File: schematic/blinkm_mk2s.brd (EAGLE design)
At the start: 15.2 x 12.7 mm, 9 parts, among them CN1 1X4SMT, Q1 MOSFET-PCHANNELIRLML2244, U1 ATTINY44QFN

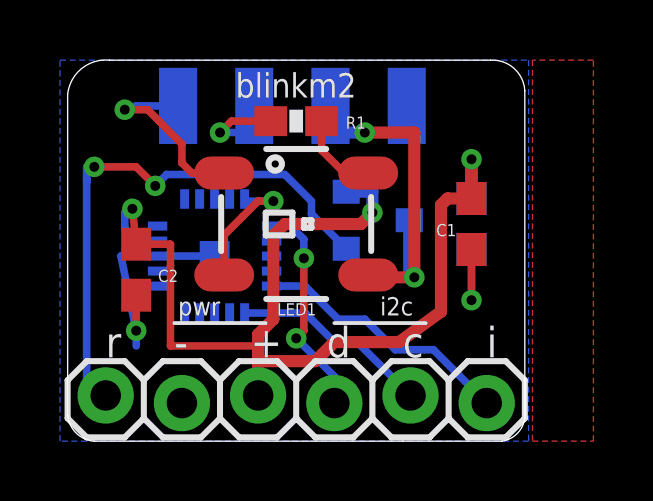
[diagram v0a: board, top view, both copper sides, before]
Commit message: blinkm2_light added patterns
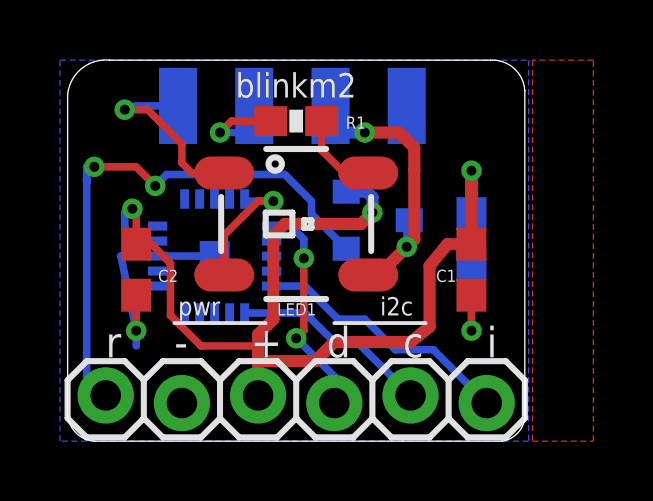
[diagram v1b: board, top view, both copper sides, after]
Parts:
- moved C1 1.52 mm to (13.7, 5.71)
- moved C3 0.51 mm to (13.7, 6.73)
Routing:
- net VCC: track 12.2 -> 10.1 mm
- net +5V: track 37.1 -> 35.9 mm

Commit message: update before sketching15
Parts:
- Q1: value MOSFET-PCHANNELIRLML2244 -> MOSFET-PCHAN
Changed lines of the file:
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@@
 <setting verticaltext="up"/>
 </settings>
-<grid distance="0.05" unitdist="inch" unit="inch" style="lines" multiple="10" display="no" altdistance="0.005" altunitdist="inch" altunit="inch"/>
+<grid distance="0.05" unitdist="inch" unit="mm" style="lines" multiple="10" display="no" altdistance="0.005" altunitdist="inch" altunit="inch"/>
 <layers>
 <layer number="1" name="Top" color="4" fill="1" visible="no" active="yes"/>
@@
 <layer number="220" name="220bmp" color="21" fill="1" visible="no" active="no"/>
 <layer number="221" name="221bmp" color="22" fill="1" visible="no" active="no"/>
-<layer number="222" name="222bmp" color="23" fill="1" visible="no" active="no"/>
 <layer number="223" name="223bmp" color="24" fill="1" visible="no" active="no"/>
 <layer number="224" name="224bmp" color="25" fill="1" visible="no" active="no"/>
@@
 </element>
 <element name="U1" library="SparkFun-DigitalIC" package="QFN20" value="ATTINY44QFN" x="5.15439375" y="6.170390625" rot="MR90"/>
-<element name="Q1" library="SparkFun-DiscreteSemi" package="SOT23-3" value="MOSFET-PCHANNELIRLML2244" x="10.541" y="7.366" smashed="yes" rot="MR90">
+<element name="Q1" library="SparkFun-DiscreteSemi" package="SOT23-3" value="MOSFET-PCHAN" x="10.541" y="7.366" smashed="yes" rot="MR90">
 <attribute name="PROD_ID" value="TRANS-11153" x="10.541" y="7.366" size="1.778" layer="28" rot="MR90" display="off"/>
 <attribute name="NAME" x="11.557" y="6.2865" size="0.4064" layer="26" rot="MR90"/>
